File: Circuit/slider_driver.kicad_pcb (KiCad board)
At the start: 2 copper layers, 99.4 x 38.5 mm, 38 parts, among them IC1 ATTINY84A-SS, P1 5_PIN_SOCKET, P10 +5V, P11 GND, P2 NEOPIXEL, P3 5_PIN_SOCKET, P4 I2C, P5 ISCP, P6 +12V, P7 GND, P8 +5V, P9 GND, SW1 RESET, U1 L9110, U2 RSA0N11M9A0J, U3 BREAK_CONNECTION, U4 74HC595-16-PIN, U5 74HC595-16-PIN

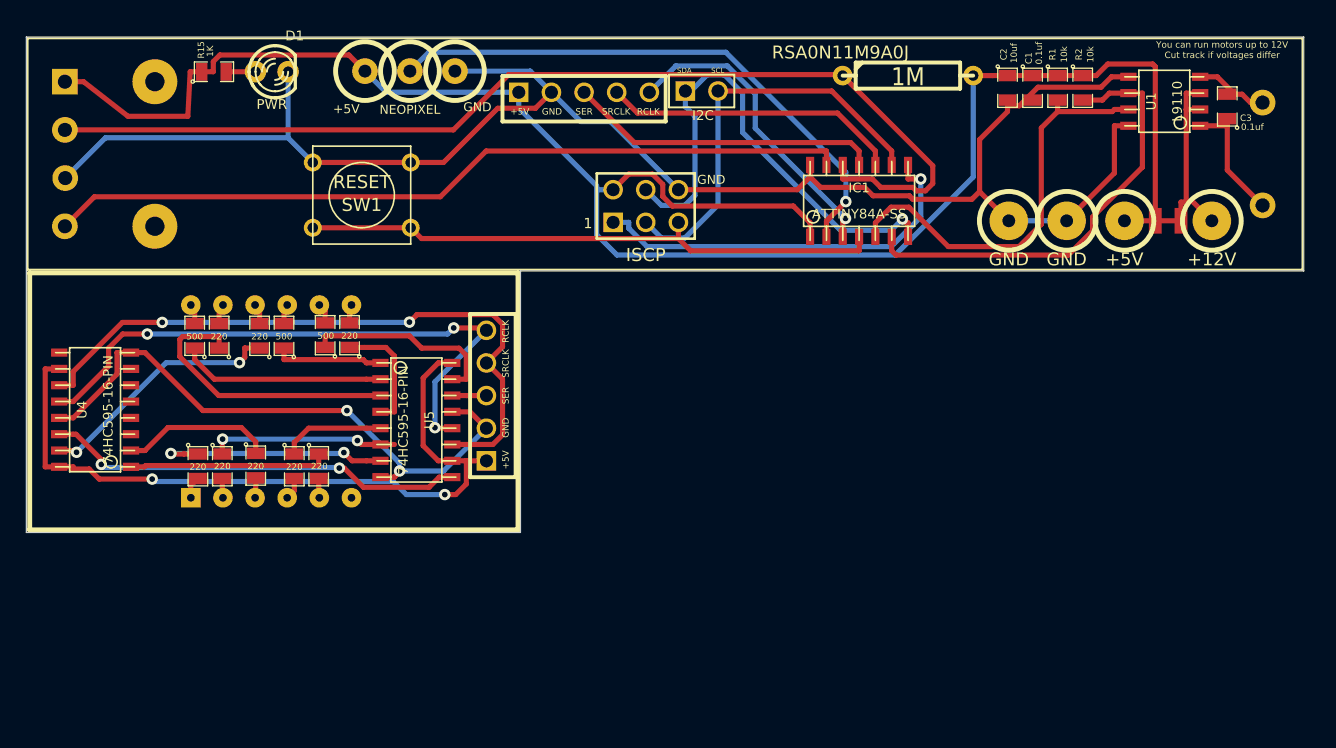
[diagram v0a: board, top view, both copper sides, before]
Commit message: Updated board to support max chip
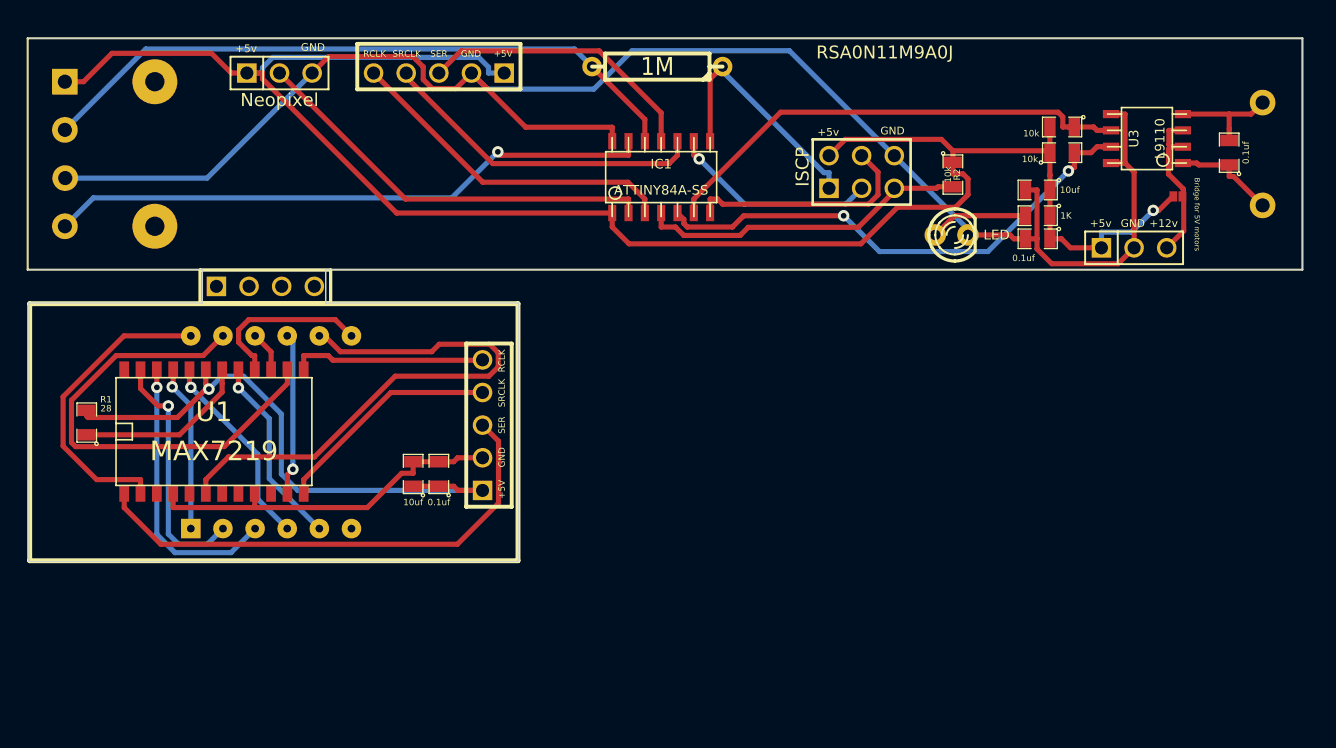
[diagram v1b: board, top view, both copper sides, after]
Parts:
- removed P10, P8: +5V, 1pin_slider
- removed P11, P7, P9: GND, 1pin_slider
- removed P5: ISCP, pin_array_3x2
- removed P6: +12V, 1pin_slider
- removed R10, R11, R6, R7, R8, R9: 220, SM0805
- removed R12, R13, R14: 500, SM0805
- removed SW1: RESET, SW_PUSH_SMALL
- removed U4, U5: 74HC595-16-PIN, so-16
- added C4: 0.1uf, SM0805, F.Cu at (44.1, 46.0)
- added C5: 10uf, SM0805, F.Cu at (42.1, 46.0)
- added K1: Neopixel, PIN_ARRAY_3X1, F.Cu at (31.7, 14.8)
- added K2: PWR, PIN_ARRAY_3X1, F.Cu at (98.2, 28.4)
- added PIN_ARRAY_4X1: Val**, PIN_ARRAY_4x1, F.Cu at (30.6, 31.4)
- AFF1: value 3X7SEGMENTS -> 3X7SEGMENTS_1
- D1: value PWR -> LED
- P2: value NEOPIXEL -> 5_PIN_SOCKET; footprint 1pin_slider -> 5pin_display
- P3: value 5_PIN_SOCKET -> ISCP; footprint 5pin_display -> pin_array_3x2
- P4: value I2C -> Bridge; footprint PIN_ARRAY_2X1 -> 603_bridge
- R1: value 10k -> 28
- R4, R5: value 220 -> 10k
- U1: value L9110 -> MAX7219; footprint so-8 -> SOIC24-WIDE
- U3: value BREAK_CONNECTION -> L9110; footprint break_connection -> so-8
- moved R1 79.9 mm to (16.7, 42.0), turned to 90 degrees
- moved U1 78.3 mm to (26.6, 42.7), turned to 0 degrees
- moved R4 67.1 mm to (92.6, 21.0), turned to 0 degrees
- moved R15 65.1 mm to (90.7, 25.9), turned to 180 degrees
- moved R5 57.8 mm to (92.6, 19.0), turned to 180 degrees
- moved D1 54.4 mm to (84.0, 27.4)
- moved P4 37.9 mm to (101.6, 24.4), turned to 180 degrees
- moved P3 34.0 mm to (77.0, 22.5), turned to 0 degrees
- moved P1 27.1 mm to (47.5, 42.2), turned to 90 degrees
- moved R3 19.5 mm to (61.1, 14.3), turned to 180 degrees
- moved IC1 15.5 mm to (61.4, 22.9)
- moved R2 12.1 mm to (84.1, 22.7)
- moved C1 11.8 mm to (90.7, 27.7), turned to 180 degrees
- moved C2 8.29 mm to (90.7, 23.9), turned to 180 degrees
- moved U3 4.70 mm to (99.2, 19.9), turned to 90 degrees
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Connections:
- net N-0000050 renamed Wiper
- AFF1 pad 1: N-0000038 -> N-0000012
- AFF1 pad 10: N-0000037 -> N-000006
- AFF1 pad 11: N-000009 -> N-000008
- AFF1 pad 12: N-000007 -> N-0000016
- AFF1 pad 2: N-0000039 -> N-000009
- AFF1 pad 3: N-0000030 -> N-0000010
- AFF1 pad 4: N-0000040 -> N-0000013
- AFF1 pad 5: N-0000031 -> N-000004
- AFF1 pad 7: N-0000035 -> N-000005
- AFF1 pad 8: N-000006 -> N-0000022
- AFF1 pad 9: N-0000036 -> N-0000017
- C1 pad 1: +12V -> +5V
- C2 pad 1: +12V -> +5V
- C3 pad 1: N-0000042 -> Motor_2
- C3 pad 2: N-0000041 -> Motor_1
- IC1 pad 1: +12V -> +5V
- IC1 pad 10: N-0000017 -> SRCLK
- IC1 pad 11: N-0000047 -> SER
- IC1 pad 12: N-0000049 -> Receive
- IC1 pad 2: N-0000048 -> N-0000029
- IC1 pad 3: N-0000016 -> RCLK
- IC1 pad 4: N-0000053 -> RESET
- IC1 pad 5: N-0000051 -> IB
- IC1 pad 6: N-0000052 -> IA
- IC1 pad 7: N-0000054 -> MOSI
- IC1 pad 8: N-0000046 -> MISO
- IC1 pad 9: N-0000045 -> SCK
- P1 pad 1: +12V -> +5V
- P1 pad 3: N-0000047 -> N-0000025
- P1 pad 4: N-0000017 -> N-0000011
- P1 pad 5: N-0000016 -> N-000001
- P2 pad 1: N-0000048 -> +5V
- P3 pad 1: N-0000015 -> MISO
- P3 pad 2: N-0000014 -> +5V
- P3 pad 3: N-0000013 -> SCK
- P3 pad 4: N-0000012 -> MOSI
- P3 pad 5: N-000002 -> RESET
- P4 pad 1: N-0000054 -> +5V
- P4 pad 2: N-0000045 -> +12V
- R1 pad 1: +12V -> N-000003
- R1 pad 2: N-0000051 -> +5V
- R15 pad 1: +12V -> +5V
- R2 pad 1: +12V -> +5V
- R2 pad 2: N-0000052 -> RESET
- R3 pad 1: N-0000049 -> MISO
- R3 pad 2: +12V -> Receive
- R4 pad 1: N-0000024 -> +5V
- R4 pad 2: N-000009 -> IB
- R5 pad 1: N-0000029 -> IA
- R5 pad 2: N-0000035 -> +5V
- U1 pad 1: N-0000042 -> N-0000025
- U1 pad 2: +12V -> N-0000016
- U1 pad 3: +12V -> (no net)
- U1 pad 4: N-0000041 -> GND
- U1 pad 5: GND -> (no net)
- U1 pad 6: N-0000052 -> N-0000022
- U1 pad 7: N-0000051 -> (no net)
- U1 pad 8: GND -> (no net)
- U2 pad 1: +12V -> +5V
- U2 pad A: N-0000041 -> Motor_1
- U2 pad B: N-0000042 -> Motor_2
- U2 pad T: N-0000049 -> Receive
- U3 pad 1: +12V -> Motor_2
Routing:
- net +5V: track 0.00 -> 190.8 mm, vias 0 -> 2
- net +12V: track 162.1 -> 12.2 mm
- net N-0000049: track 82.3 -> 0.00 mm
- net N-0000015: track 58.2 -> 0.00 mm, vias 2 -> 0
- net Receive: track 0.00 -> 51.7 mm
- net N-000002: track 47.1 -> 0.00 mm, vias 3 -> 0
- net N-0000014: track 46.8 -> 0.00 mm, vias 2 -> 0
- net N-0000053: track 45.6 -> 0.00 mm
- net N-0000048: track 44.0 -> 0.00 mm, vias 1 -> 0
- net IB: track 0.00 -> 39.9 mm, vias 0 -> 2
- net N-0000054: track 39.5 -> 0.00 mm, vias 1 -> 0
- net N-0000012: track 51.6 -> 13.0 mm, vias 2 -> 1
- net IA: track 0.00 -> 37.4 mm
- net N-0000052: track 34.8 -> 0.00 mm
- net N-0000045: track 32.6 -> 0.00 mm
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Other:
- board size 99.4 x 38.5 mm -> 99.2 x 40.7 mm
- board text added: "+12v"
- board text added: "+5v"
- board text added: "Bridge for 5V motors"
- board text added: "RSA0N11M9A0J motor driver board V1.2 https://github.com/mage0r/RSA0N11M9A0J_motorised_slider John Spencer 2015 Made at hackmelbourne.org"
- board text removed: "1"
- board text removed: "Controller for RSA0N11M9A0J motorised slider Designed by John Spencer, 2014 https://github.com/mage0r/RSA0N11M9A0J_motorised_slider Version 1.3"
- board text removed: "SCL"
- board text removed: "SDA"
- board text removed: "You can run motors up to 12V Cut track if voltages differ"

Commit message: Adaption to make fab people happy.
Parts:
- removed PIN_ARRAY_4X1: Val**, PIN_ARRAY_4x1
- moved AFF1 12.4 mm to (31.0, 55.1)
- moved C4 12.4 mm to (44.1, 58.4)
- moved C5 12.4 mm to (42.1, 58.4)
- moved P1 12.4 mm to (47.5, 54.6)
- moved R1 12.4 mm to (16.7, 54.4)
- moved U1 12.4 mm to (26.6, 55.1)
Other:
- board size 99.2 x 40.7 mm -> 99.2 x 53.1 mm
